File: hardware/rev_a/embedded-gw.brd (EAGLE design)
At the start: 34.5 x 58 mm, 42 parts, among them J1 DM3BT-DSF-PEJS, J2 USB-A-MALE-PLUG, J3 TC2030-JLINK-NL, U1 ESP32-WROVER-E, U2 ESP32-WROVER-E, U3 AP7362A-33SP-13, U4 BC840M, U5 CP2102N-20, U6 ESDR0502N

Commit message: forgot to save
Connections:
- removed net VSPIHD: U1.33
- removed net VSPIWP: U1.36
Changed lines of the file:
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@@
 <wire x1="16.63" y1="18.9" x2="16.64" y2="38.4" width="0" layer="19" extent="1-1"/>
-</signal>
-<signal name="VSPIWP">
-<contactref element="U1" pad="36"/>
-</signal>
-<signal name="VSPIHD">
-<contactref element="U1" pad="33"/>
 </signal>
 <signal name="ESP32_MOSI">

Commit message: start layout
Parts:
- removed D11: YELLOW, leds:LED-0603
- removed D12: BLUE, leds:LED-0603
- removed U4: BC840M, chips:BC840M
- added C12, C13: 12pF, passives:0402_CAP
- added D10: BLUE, leds:LED-0603
- added D9: YELLOW, leds:LED-0603
- added R10, R8: 10k, passives:0402_RES
- added U7: BT840X, BT840X:XCVR_BT840X
- added X1: ABS05-32.768KHZ-9-T, crystals:ABS05
- C5, C6, C7: device passives:0402_CAP -> passives:0805_CAP
- D3: value BLUE -> YELLOW
- D4, D7: value YELLOW -> BLUE
- D5: value BLUE -> RED
- D6: value RED -> YELLOW
- moved R7 182.7 mm to (23.5, 52.5), flipped to the bottom, turned to 270 degrees
- moved D5 178.2 mm to (31.0, 53.0), flipped to the bottom, turned to 180 degrees
- moved R3 175.7 mm to (15.0, 52.5), turned to 270 degrees
- moved D8 169.3 mm to (16.5, 28.5), turned to 270 degrees
- moved R11 168.8 mm to (16.0, 30.0), turned to 180 degrees
- moved D3 168.1 mm to (10.5, 53.0), turned to 180 degrees
- moved R13 167.0 mm to (16.0, 24.0), turned to 180 degrees
- moved R12 164.7 mm to (16.0, 27.0), turned to 180 degrees
- moved R6 156.5 mm to (26.5, 52.5), flipped to the bottom, turned to 270 degrees
- moved R5 154.3 mm to (29.5, 52.5), flipped to the bottom, turned to 270 degrees
- moved R4 143.4 mm to (12.0, 52.5), turned to 270 degrees
- moved D7 141.2 mm to (25.0, 53.0), flipped to the bottom, turned to 180 degrees
- moved D6 134.3 mm to (28.0, 53.0), flipped to the bottom, turned to 180 degrees
- moved R2 121.9 mm to (9.00, 52.5), turned to 270 degrees
- moved D4 109.9 mm to (13.5, 53.0), turned to 180 degrees
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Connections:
- net N$1 renamed RXD
- net N$2 renamed TXD
- net N$4 renamed D+
- net N$5 renamed D-
- removed net ESP32_MISO: U1.31, U2.31
- removed net ESP32_MOSI: U1.37, U2.37
- removed net ESP32_SCLK: U1.30, U2.30
- removed net NRF_HANDSHAKE: U2.10, U4.A0
- new net DCCH: U7.F5
- new net ESP32_0_ID: R8.2, U1.11
- new net ESP32_1_ID: R10.1, U2.11
- new net N$1: U7.F6
- new net N$2: C12.2, U7.3, X1.B
- new net VBUS: C1.1, C2.1, C5.P$1, J2.P$1, U3.2, U3.3, U3.4, U5.7, U5.8, U6.P$6
- net !RESET: now also U7.14; no longer U4.B4
- net !SD_INSERTED: now also U1.12, U2.12
- net ESP32_CS: now also U1.10, U2.10; no longer U1.29, U2.29
- net GND: now also C12.1, C13.1, C5.P$2, C6.P$2, C7.P$2, R8.1, U7.10, U7.A0, U7.B0, U7.C0, U7.D0, U7.F0, U7.F1, U7.F2, U7.F3; no longer C5.2, C6.2, C7.2, U4.G0, U4.G4, U4.G5, U4.G6, U4.H4, U4.H5, U4.H6, U4.H7
- net LED10: no longer R11.2
- net LED11: no longer R12.2
- net LED12: no longer R13.2
- net N$14: now also D3.C; no longer D4.C
- net N$15: now also D4.C; no longer D3.C
- net N$19: now also D5.C; no longer D6.C
- net N$20: now also D6.C; no longer D7.C
- net N$21: now also D7.C; no longer D5.C
- net N$23: now also D9.C; no longer D11.C
- net N$24: now also D10.C; no longer D12.C
- net N$3: now also C13.2, U7.4, X1.A; no longer C1.1, C2.1, C5.1, J2.P$1, U3.2, U3.3, U3.4, U5.7, U5.8, U6.P$6
- net NRF_CS: now also U1.29, U2.29, U7.E1; no longer U2.16, U4.A1
- net NRF_LED0: now also R11.2, U7.13; no longer U4.E5
- net NRF_LED1: now also R12.2, U7.D4; no longer U4.E6
- net NRF_LED2: now also R13.2, U7.C4; no longer U4.E7
- net NRF_MISO: now also U1.31, U2.31, U7.E2; no longer U2.24, U4.C6
- net NRF_MOSI: now also U1.37, U2.37, U7.C2; no longer U2.23, U4.C7
- net NRF_SCLK: now also U1.30, U2.30, U7.D2; no longer U2.13, U4.B7
- net SD_HOST_CLK: now also U2.13
- net SD_HOST_CMD: now also U2.23
- net SD_HOST_D0: now also U2.24
- net SD_HOST_D1: now also U2.26
- net SD_HOST_D2: now also U2.14
- net SD_HOST_D3: now also U2.16
- net SWDCLK: now also U7.15; no longer U4.C1
- net SWDIO: now also U7.16; no longer U4.B1
- net VCC: now also C6.P$1, C7.P$1, D10.A, D9.A, R10.2, U7.9, U7.F4; no longer C6.1, C7.1, D11.A, D12.A, U4.A7, U4.F5
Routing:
- net NRF_MOSI: track 0.00 -> 67.7 mm, vias 0 -> 4
- net NRF_SCLK: track 0.00 -> 58.5 mm, vias 0 -> 2
- net ESP32_1_TXD: track 0.00 -> 58.0 mm, vias 0 -> 2
- net ESP32_1_RXD: track 0.00 -> 57.4 mm, vias 0 -> 2
- net NRF_MISO: track 0.00 -> 54.8 mm, vias 0 -> 2
- net NRF_CS: track 0.00 -> 50.8 mm, vias 0 -> 3
- net SD_HOST_CMD: track 0.00 -> 46.7 mm, vias 0 -> 3
- net SD_HOST_D0: track 0.00 -> 43.6 mm, vias 0 -> 3
- net SD_HOST_D1: track 0.00 -> 39.6 mm, vias 0 -> 3
- net ESP32_0_RXD: track 0.00 -> 37.0 mm, vias 0 -> 1
- net SD_HOST_D3: track 0.00 -> 31.2 mm, vias 0 -> 1
- net ESP32_0_TXD: track 0.00 -> 30.2 mm, vias 0 -> 1
- net D-: track 0.00 -> 28.2 mm
- net SD_HOST_D2: track 0.00 -> 26.3 mm, vias 0 -> 1
- net LED02: track 0.00 -> 24.1 mm
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- added copper zone on layer 1, net GND
- added copper zone on layer 16, net GND
- added copper zone on layer 2, net GND
- added copper zone on layer 15, net VBUS
- added copper zone on layer 16, net VBUS
- added copper zone on layer 1, net VCC
- added copper zone on layer 15, net VCC
- added copper zone on layer 16, net VCC
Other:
- board size 34.5 x 58 mm -> 38.5 x 56 mm

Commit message: nothing to do
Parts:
- moved R9 36.3 mm to (28.5, 44.5), flipped to the bottom, turned to 0 degrees
- moved U1 30.4 mm to (7.00, 50.0), turned to 270 degrees
- moved R8 25.5 mm to (22.0, 52.5), turned to 270 degrees
- moved R10 22.0 mm to (28.5, 46.0), flipped to the bottom, turned to 180 degrees
- moved D2 22.0 mm to (29.5, 53.0)
- moved R2 22.0 mm to (31.0, 52.5)
- moved U2 18.5 mm to (25.5, 31.0), turned to 0 degrees
- moved D3 16.0 mm to (26.5, 53.0)
- moved R4 16.0 mm to (28.0, 52.5)
- moved R11 15.9 mm to (4.50, 19.0), turned to 0 degrees
- moved D8 14.8 mm to (4.00, 20.5), turned to 90 degrees
- moved D10 13.1 mm to (4.00, 26.5), turned to 90 degrees
- moved D9 12.7 mm to (4.00, 23.5), turned to 90 degrees
- moved R12 12.5 mm to (4.50, 22.0), turned to 0 degrees
- moved S2 12.5 mm to (1.50, 35.0)
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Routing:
- net !SD_INSERTED: track 7.05 -> 55.3 mm
- net ESP32_1_TXD: track 58.0 -> 25.8 mm
- net ESP32_1_RXD: track 57.4 -> 25.6 mm, vias 2 -> 0
- net SD_HOST_CMD: track 46.7 -> 19.9 mm
- net NRF_LED0: track 0.00 -> 26.2 mm, vias 0 -> 2
- net SD_HOST_D0: track 43.6 -> 20.9 mm
- net SD_HOST_CLK: track 21.6 -> 41.8 mm, vias 3 -> 2
- net LED02: track 24.1 -> 4.08 mm
- net NRF_LED2: track 1.04 -> 20.9 mm, vias 1 -> 2
- net SD_HOST_D2: track 26.3 -> 44.8 mm
- net NRF_LED1: track 1.04 -> 19.4 mm, vias 1 -> 2
- net LED01: track 23.9 -> 5.77 mm
- net LED12: track 22.1 -> 4.58 mm
- net LED11: track 21.1 -> 6.17 mm
- net LED00: track 22.5 -> 8.19 mm
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
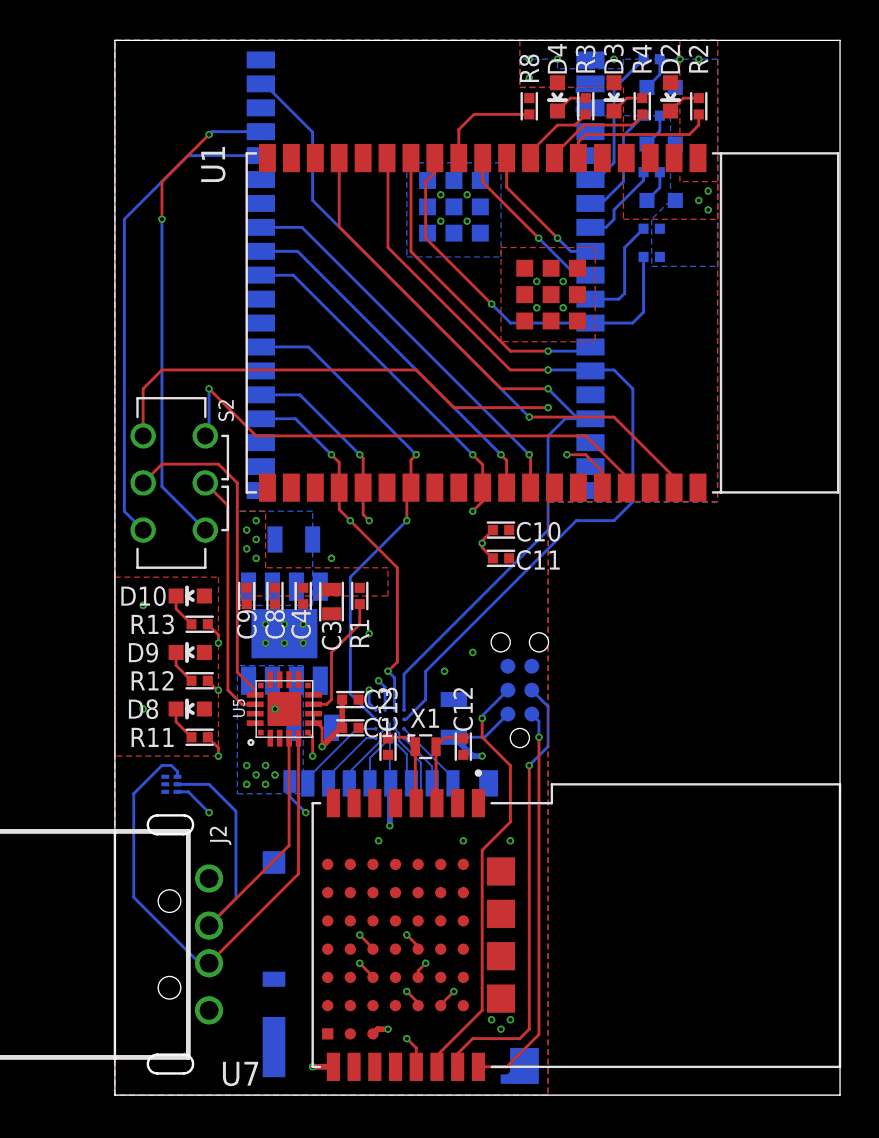
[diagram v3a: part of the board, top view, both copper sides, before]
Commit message: fix labels
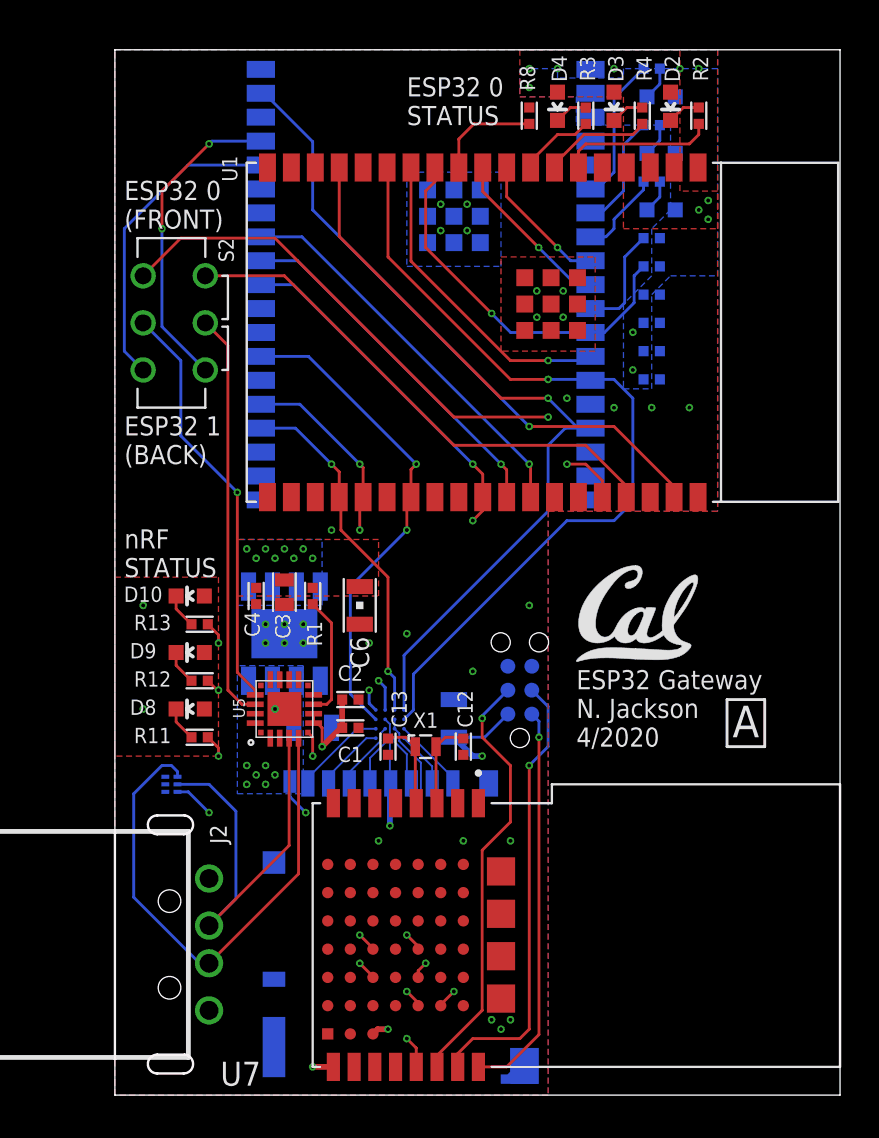
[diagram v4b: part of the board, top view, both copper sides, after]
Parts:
- added U$4: (no value), logos:UCB_CAL_200MIL
- moved C9 25.1 mm to (28.5, 39.5), flipped to the bottom, turned to 180 degrees
- moved C8 23.1 mm to (28.5, 38.0), flipped to the bottom, turned to 180 degrees
- moved C11 16.1 mm to (28.5, 42.5), flipped to the bottom, turned to 180 degrees
- moved C10 13.6 mm to (28.5, 41.0), flipped to the bottom, turned to 180 degrees
- moved S2 8.50 mm to (1.50, 43.5)
- moved C6 4.95 mm to (13.0, 26.0), flipped to the top, turned to 90 degrees
- moved C3 2.55 mm to (9.00, 26.7)
- moved C4 2.50 mm to (7.50, 26.5)
- moved R1 2.50 mm to (10.5, 26.5)
- moved D2 0.50 mm to (29.5, 52.5)
- moved D3 0.50 mm to (26.5, 52.5)
- moved D4 0.50 mm to (23.5, 52.5)
- moved D5 0.50 mm to (29.0, 53.0)
- moved D6 0.50 mm to (29.0, 50.0)
- moved D7 0.50 mm to (29.0, 47.0)
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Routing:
- net ESP32_1_RXD: track 25.6 -> 16.6 mm
- net ESP32_1_TXD: track 25.8 -> 16.8 mm
- net TXD: track 13.3 -> 21.8 mm
- net RXD: track 17.5 -> 22.2 mm, vias 0 -> 1
- net VCC: track 16.4 -> 14.4 mm, vias 20 -> 24
- net !SD_INSERTED: track 55.3 -> 53.9 mm
- net ESP32_0_RXD: track 31.3 -> 32.3 mm
- net NRF_MOSI: track 69.0 -> 68.1 mm
- net SD_HOST_CMD: track 19.9 -> 19.0 mm, vias 3 -> 2
- net SD_HOST_D0: track 20.9 -> 20.1 mm
- net NRF_SCLK: track 48.7 -> 48.2 mm
- net SD_HOST_D3: track 41.6 -> 41.1 mm
- net SD_HOST_D1: track 26.7 -> 26.2 mm
- net SD_HOST_CLK: track 41.8 -> 41.3 mm
- net NRF_MISO: track 56.4 -> 55.9 mm
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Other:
- board size 38.5 x 56 mm -> 38.5 x 55.5 mm
- board text added: ">REV"
- board text added: "ESP32 0 (FRONT)"
- board text added: "ESP32 0 STATUS"
- board text added: "ESP32 1 (BACK)"
- board text added: "ESP32 1 STATUS"
- board text added: "ESP32 Gateway N. Jackson 4/2020"
- board text added: "nRF STATUS"

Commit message: Clean up and run the script
rename parts, clean up bom, cam, package up
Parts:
- removed U7: BT840X, BT840X:XCVR_BT840X
- added D11: BLUE, leds:LED-0603
- added U4: ESDR0502N, chips:UDFN-6
- C1: value 1.0uF -> 12pF
- C10: value 1.0uF -> 4.7uF; device passives:0402_CAP -> passives:0603_CAP
- C11: value 0.1uF -> 10uF; device passives:0402_CAP -> passives:0805_CAP
- C12, C13: value 12pF -> 10uF; device passives:0402_CAP -> passives:0805_CAP
- C2: value 0.1uF -> 12pF
- C3: value 4.7uF -> 0.1uF; device passives:0603_CAP -> passives:0402_CAP
- C5, C6: value 10uF -> 0.1uF; device passives:0805_CAP -> passives:0402_CAP
- C7: value 10uF -> 1.0uF; device passives:0805_CAP -> passives:0402_CAP
- C9: value 0.1uF -> 1.0uF
- D1: value EMIF06-MSD01F2 -> (none); device passives:BGA16C50P4X4_192X192X65N -> passives:0201_DIODE
- D10, D4: value BLUE -> YELLOW
- D2: value RED -> EMIF06-MSD01F2; device leds:LED-0603 -> passives:BGA16C50P4X4_192X192X65N
- D3, D9: value YELLOW -> RED
- D8: value RED -> BLUE
- J2: value USB-A-MALE-PLUG -> TC2030-JLINK-NL; device connector:USB_A_MALE_PLUG_CUI_UP2-AH -> connector:TC2030-IDC-NL
- J3: value TC2030-JLINK-NL -> USB-A-MALE-PLUG; device connector:TC2030-IDC-NL -> connector:USB_A_MALE_PLUG_CUI_UP2-AH
- R1: value 10k -> 100
- R11, R12: value 470 -> 10k
- R13: value 100 -> 10k
- R2: value 470 -> 100
- R7: value 100 -> 470
- R8, R9: value 10k -> 470
- U1: value ESP32-WROVER-E -> AP7362A-33SP-13; device chips:ESP32-WROVER-E -> chips:SO-8EP
- U2: value ESP32-WROVER-E -> BT840X; device chips:ESP32-WROVER-E -> BT840X:XCVR_BT840X
- U3: value AP7362A-33SP-13 -> CP2102N-20; device chips:SO-8EP -> chips:QFN-20-3MM
- U5: value CP2102N-20 -> ESP32-WROVER-E; device chips:QFN-20-3MM -> chips:ESP32-WROVER-E
- U6: value ESDR0502N -> ESP32-WROVER-E; device chips:UDFN-6 -> chips:ESP32-WROVER-E
- moved R8 37.4 mm to (4.50, 19.0), turned to 0 degrees
- moved D8 36.4 mm to (29.0, 47.0), flipped to the bottom, turned to 270 degrees
- moved D2 36.0 mm to (14.6, 19.7), flipped to the bottom, turned to 270 degrees
- moved R12 34.7 mm to (22.0, 52.0), turned to 270 degrees
- moved R11 34.7 mm to (28.5, 44.0), flipped to the bottom
- moved R3 33.9 mm to (4.50, 25.0), turned to 0 degrees
- moved R9 32.6 mm to (4.50, 22.0), flipped to the top
- moved R13 31.6 mm to (28.5, 45.5), flipped to the bottom, turned to 180 degrees
- moved R1 29.3 mm to (25.0, 52.0), turned to 270 degrees
- moved C11 29.2 mm to (10.5, 19.5), turned to 0 degrees
- moved U5 29.1 mm to (7.00, 49.5), turned to 270 degrees
- moved C5 26.9 mm to (28.5, 39.5), turned to 180 degrees
- moved U6 26.5 mm to (25.5, 30.5), turned to 0 degrees
- moved R10 26.2 mm to (10.5, 26.5), flipped to the top, turned to 90 degrees
- moved J2 25.4 mm to (21.5, 21.5), flipped to the bottom, turned to 90 degrees
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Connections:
- removed net N$1: U7.F6
- removed net N$12 (its old number): D2.C, R2.1
- new net N$14: D4.C, R5.1
- new net NC: U2.F6
- net !RESET: now also J2.3, U2.14; no longer J3.3, U7.14
- net !SD_INSERTED: now also D1.P$1, R11.2, U5.12, U6.12; no longer R9.2, U1.12, U2.12
- net D+: now also J3.P$3, U3.4, U4.P$5; no longer J2.P$3, U5.4, U6.P$5
- net D-: now also J3.P$2, U3.5, U4.P$4; no longer J2.P$2, U5.5, U6.P$4
- net DCCH: now also U2.F5; no longer U7.F5
- net ESP32_0_ID: now also R12.2, U5.11; no longer R8.2, U1.11
- net ESP32_0_RXD: now also U5.34; no longer U1.34
- net ESP32_0_TXD: now also U5.35; no longer U1.35
- net ESP32_1_ID: now also R13.1, U6.11; no longer R10.1, U2.11
- net ESP32_1_RXD: now also U6.34; no longer U2.34
- net ESP32_1_TXD: now also U6.35; no longer U2.35
- net ESP32_CS: now also U5.10, U6.10; no longer U1.10, U2.10
- net ESP32_HANDSHAKE: now also U5.9, U6.9; no longer U1.9, U2.9
- net GND: now also C1.1, C11.P$2, C12.P$2, C13.P$2, C2.1, C5.2, C6.2, C7.2, D1.P$2, D2.B3, D2.C2, D2.C3, J2.5, J3.P$4, R12.1, U1.PAD, U2.10, U2.A0, U2.B0, U2.C0, U2.D0, U2.F0, U2.F1, U2.F2, U2.F3, U3.12, U3.3, U3.P$1, U4.P$1, U5.1, U5.15, U5.38, U5.GND1, U5.GND2, U5.GND3, U5.GND4, U5.GND5, U5.GND6, U5.GND7, U5.GND8, U5.GND9, U6.1, U6.15, U6.38, U6.GND1, U6.GND2, U6.GND3, U6.GND4, U6.GND5, U6.GND6, U6.GND7, U6.GND8, U6.GND9; no longer C1.2, C11.2, C12.1, C13.1, C2.2, C5.P$2, C6.P$2, C7.P$2, D1.B3, D1.C2, D1.C3, J2.P$4, J3.5, R8.1, U1.15, U1.38, U1.GND1, U1.GND2, U1.GND3, U1.GND4, U1.GND5, U1.GND6, U1.GND7, U1.GND8, U1.GND9, U2.1, U2.15, U2.38, U2.GND1, U2.GND2, U2.GND3, U2.GND4, U2.GND5, U2.GND6, U2.GND7, U2.GND8, U2.GND9, U3.1, U3.PAD, U5.12, U5.3, U5.P$1, U6.P$1, U7.10, U7.A0, U7.B0, U7.C0, U7.D0, U7.F0, U7.F1, U7.F2, U7.F3
- net LED00: now also R4.2, U5.6; no longer R2.2, U1.6
- net LED01: now also R5.2, U5.7; no longer R4.2, U1.7
- net LED02: now also R1.2, U5.8; no longer R3.2, U1.8
- net LED10: now also R6.2, U6.6; no longer R5.2, U2.6
- net LED11: now also R7.2, U6.7; no longer R6.2, U2.7
- net LED12: now also R2.2, U6.8; no longer R7.2, U2.8
- net N$10: now also D2.D3; no longer D1.D3
- net N$11: now also D2.D4; no longer D1.D4
- net N$13: now also D2.B4; no longer D1.B4
- net N$15: now also D7.C, R1.1; no longer D4.C, R3.1
- net N$19: now also R6.1; no longer R5.1
- net N$2: now also C1.2, U2.3; no longer C12.2, U7.3
- net N$20: now also R7.1; no longer R6.1
- net N$21: now also D8.C, R2.1; no longer D7.C, R7.1
- net N$22: now also D9.C, R8.1; no longer D8.C, R11.1
- net N$23: now also D10.C, R9.1; no longer D9.C, R12.1
- net N$24: now also D11.C, R3.1; no longer D10.C, R13.1
- net N$3: now also C2.2, U2.4; no longer C13.2, U7.4
- net N$6: now also D2.C4; no longer D1.C4
- net N$7: now also R10.1, U3.9; no longer R1.1, U5.9
- net N$8: now also D2.A4; no longer D1.A4
- net N$9: now also D2.A3; no longer D1.A3
- net NRF_CS: now also U2.E1, U5.29, U6.29; no longer U1.29, U2.29, U7.E1
- net NRF_LED0: now also R8.2, U2.13; no longer R11.2, U7.13
- net NRF_LED1: now also R9.2, U2.D4; no longer R12.2, U7.D4
- net NRF_LED2: now also R3.2, U2.C4; no longer R13.2, U7.C4
- net NRF_MISO: now also U2.E2, U5.31, U6.31; no longer U1.31, U2.31, U7.E2
- net NRF_MOSI: now also U2.C2, U5.37, U6.37; no longer U1.37, U2.37, U7.C2
- net NRF_SCLK: now also U2.D2, U5.30, U6.30; no longer U1.30, U2.30, U7.D2
- net RXD: now also U3.17; no longer U5.17
- net SD_HOST_CLK: now also D2.B1, U5.13, U6.13; no longer D1.B1, U1.13, U2.13
- net SD_HOST_CMD: now also D2.C1, U5.23, U6.23; no longer D1.C1, U1.23, U2.23
- net SD_HOST_D0: now also D2.A1, U5.24, U6.24; no longer D1.A1, U1.24, U2.24
- net SD_HOST_D1: now also D2.A2, U5.26, U6.26; no longer D1.A2, U1.26, U2.26
- net SD_HOST_D2: now also D2.D2, U5.14, U6.14; no longer D1.D2, U1.14, U2.14
- net SD_HOST_D3: now also D2.D1, U5.16, U6.16; no longer D1.D1, U1.16, U2.16
- net SWDCLK: now also J2.4, U2.15; no longer J3.4, U7.15
- net SWDIO: now also J2.2, U2.16; no longer J3.2, U7.16
- net TXD: now also U3.18; no longer U5.18
- net VBUS: now also C11.P$1, C3.1, C7.1, J3.P$1, U1.2, U1.3, U1.4, U3.7, U3.8, U4.P$6; no longer C1.1, C2.1, C5.P$1, J2.P$1, U3.2, U3.3, U3.4, U5.7, U5.8, U6.P$6
- net VCC: now also C12.P$1, C13.P$1, C5.1, C6.1, D11.A, D2.B2, J2.1, R11.1, R13.2, U1.5, U1.6, U1.7, U2.9, U2.F4, U5.2, U5.3, U6.2, U6.3; no longer C11.1, C3.1, C6.P$1, C7.P$1, D1.B2, D2.A, J3.1, R1.2, R9.1, U1.2, U1.3, U2.2, U2.3, U3.5, U3.7, U5.6, U7.9, U7.F4
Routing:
- net !SD_INSERTED: track 53.9 -> 57.6 mm
- net GND: track 8.97 -> 6.77 mm, vias 32 -> 39
- net N$14: track 0.00 -> 1.78 mm
- net N$12 (its old number): track 1.78 -> 0.00 mm
